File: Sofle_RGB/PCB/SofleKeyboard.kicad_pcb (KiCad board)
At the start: 2 copper layers, 143.4 x 111.8 mm, 97 parts, among them J1 LED, J2 4PIN, J3 OLED, J4 key leds, J5 backlight sel, J6 indicator bypass, P1 i2c_pin, P2 i2c_pin, SW1 SW_PUSH-MX_W_LED, SW10 SW_PUSH-MX_W_LED, SW11 SW_PUSH-MX_W_LED, SW12 SW_PUSH-MX_W_LED, SW13 SW_PUSH-MX_W_LED, SW14 SW_PUSH-MX_W_LED, SW15 SW_PUSH-MX_W_LED, SW16 SW_PUSH-MX_W_LED, SW17 SW_PUSH-MX_W_LED, SW18 SW_PUSH-MX_W_LED, SW19 SW_PUSH-MX_W_LED, SW2 SW_PUSH-MX_W_LED, SW20 SW_PUSH-MX_W_LED, SW21 SW_PUSH-MX_W_LED, SW22 SW_PUSH-MX_W_LED, SW23 SW_PUSH-MX_W_LED, SW24 SW_PUSH-MX_W_LED, SW25 Rotary_Encoder_Switch, SW26 SW_PUSH-MX_W_LED, SW27 SW_PUSH-MX_W_LED, SW28 SW_PUSH-MX_W_LED, SW29 SW_PUSH-MX_W_LED, SW3 SW_PUSH-MX_W_LED, SW30 SW_PUSH-MX_W_LED, SW4 SW_PUSH-MX_W_LED, SW5 SW_PUSH-MX_W_LED, SW6 SW_PUSH-MX_W_LED, SW7 SW_PUSH-MX_W_LED, SW8 SW_PUSH-MX_W_LED, SW9 SW_PUSH-MX_W_LED, U1 ProMicro

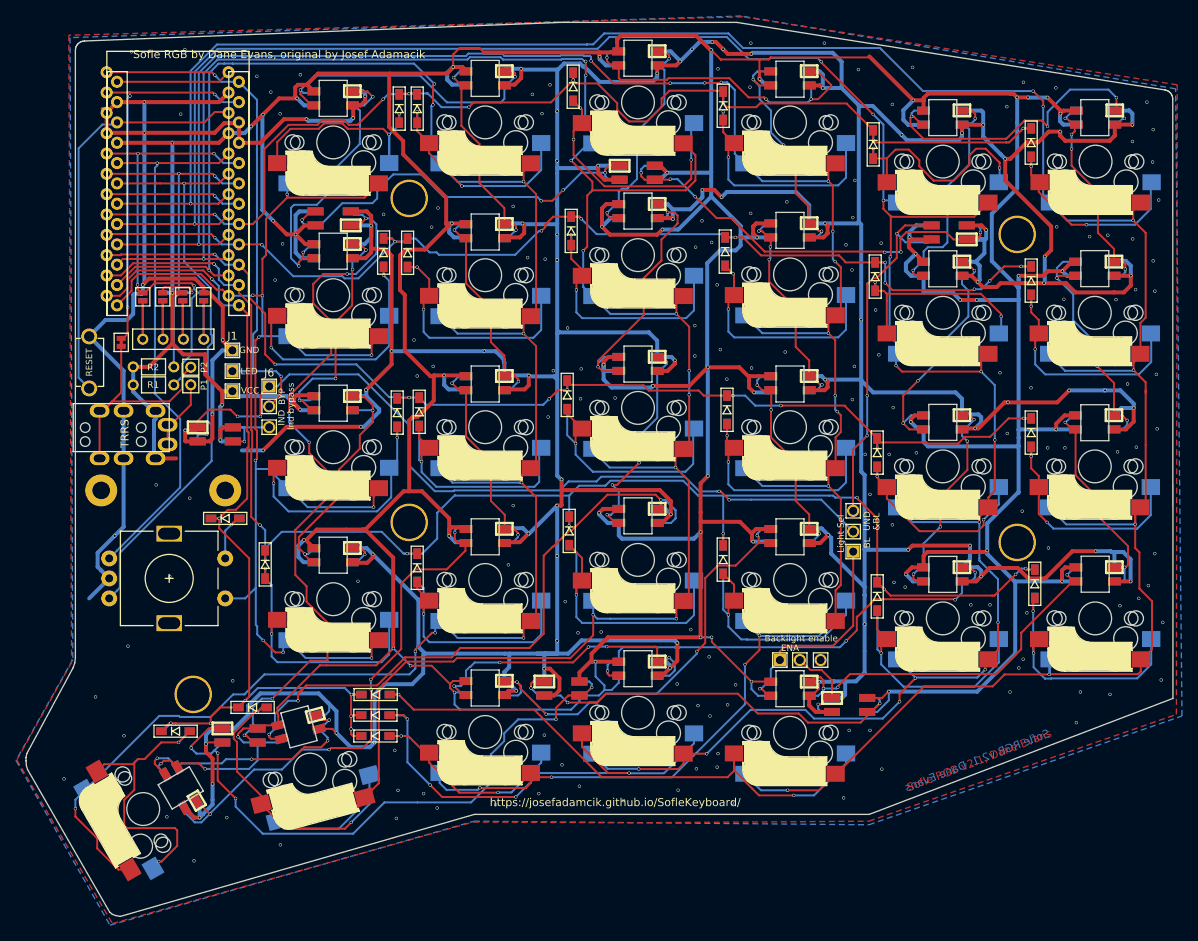
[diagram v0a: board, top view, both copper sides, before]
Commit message: Cleaned and retraced some GND tracks.
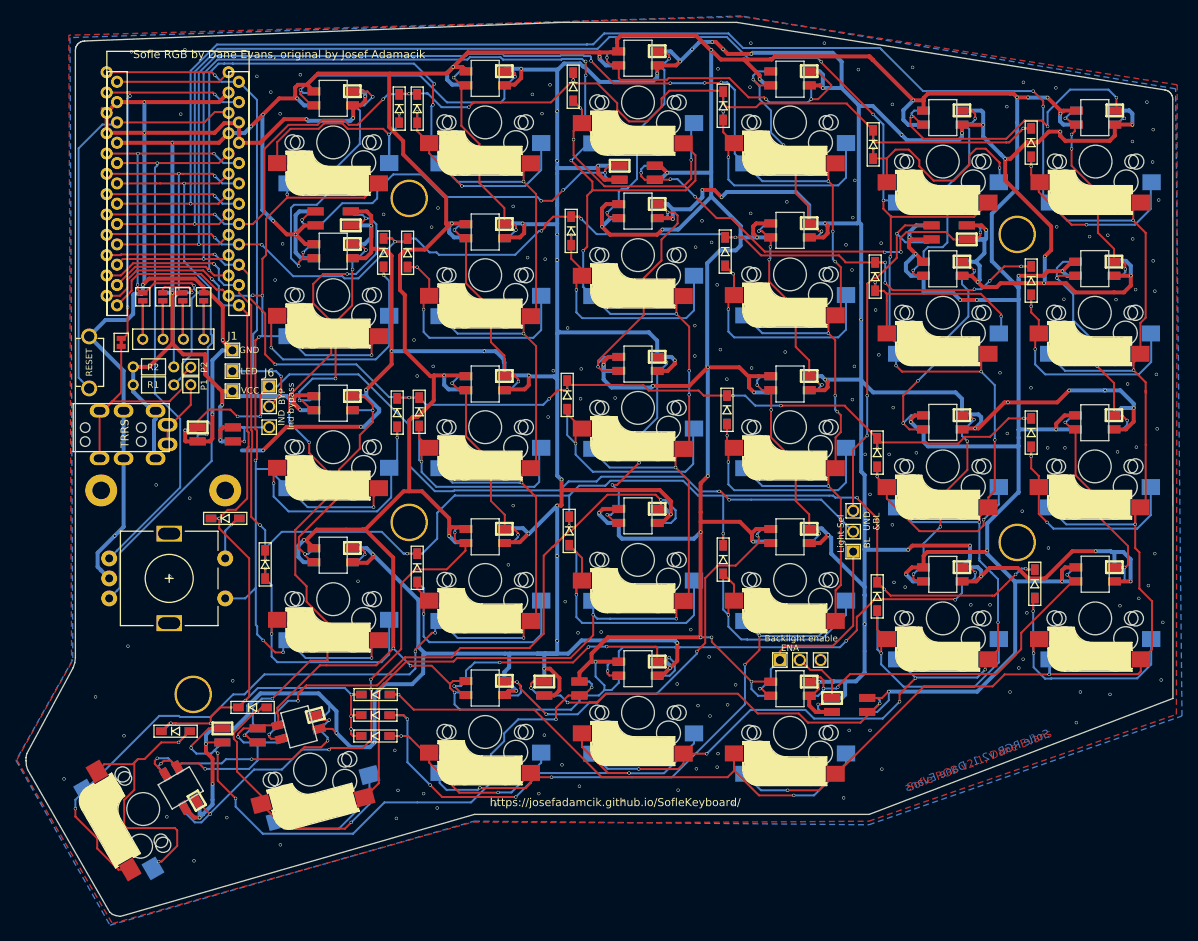
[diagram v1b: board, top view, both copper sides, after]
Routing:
- net VCC: track 928.4 -> 923.7 mm
- net GND: track 1001.1 -> 997.6 mm
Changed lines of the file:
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@@
     (thickness 1.6)
     (drawings 363)
-    (tracks 3681)
+    (tracks 3672)
     (zones 0)
     (modules 97)
@@
     (visible_elements 7FFFF7FF)
     (pcbplotparams
-      (layerselection 0x010f0_ffffffff)
+      (layerselection 0x010fc_ffffffff)
       (usegerberextensions true)
       (usegerberattributes false)
@@
       (psa4output false)
       (plotreference true)
-      (plotvalue true)
+      (plotvalue false)
       (plotinvisibletext false)
       (padsonsilk false)
-      (subtractmaskfromsilk false)
+      (subtractmaskfromsilk true)
       (outputformat 1)
       (mirror false)
@@
   (segment (start 134.749998 41.325012) (end 135.5 40.57501) (width 0.5) (layer B.Cu) (net 33))
   (via (at 153.8 39.29) (size 0.4) (drill 0.3) (layers F.Cu B.Cu) (net 33))
-  (segment (start 193.0125 44.7375) (end 187.525 39.25) (width 0.5) (layer F.Cu) (net 33))
   (via (at 173.806234 42.08623) (size 0.4) (drill 0.3) (layers F.Cu B.Cu) (net 33))
   (segment (start 174.595004 42.875) (end 173.841595 42.121591) (width 0.5) (layer B.Cu) (net 33))
   (segment (start 175.2 42.875) (end 174.595004 42.875) (width 0.5) (layer B.Cu) (net 33))
-  (segment (start 173.785002 42.064998) (end 173.806234 42.08623) (width 0.5) (layer F.Cu) (net 33))
-  (segment (start 173.785002 41.814998) (end 173.785002 42.064998) (width 0.5) (layer F.Cu) (net 33))
   (segment (start 118.1 83.475) (end 116.425 83.475) (width 0.5) (layer B.Cu) (net 33))
   (segment (start 114.662001 81.712001) (end 116.35 83.4) (width 0.5) (layer B.Cu) (net 33))
@@
   (segment (start 200.95 69.7) (end 206.1 69.7) (width 0.5) (layer B.Cu) (net 33))
   (segment (start 206.175 68.125) (end 206.175 85.925) (width 0.5) (layer B.Cu) (net 33))
-  (segment (start 167.75 38.44) (end 168.946 39.636) (width 0.25) (layer F.Cu) (net 33))
-  (segment (start 168.946 39.636) (end 168.946 39.65) (width 0.25) (layer F.Cu) (net 33))
   (segment (start 135.225 60.125) (end 135.325 60.125) (width 0.5) (layer F.Cu) (net 33))
   (segment (start 129.569998 63.4) (end 131.95 63.4) (width 0.5) (layer F.Cu) (net 33))
@@
   (segment (start 153.782 39.272) (end 153.8 39.29) (width 0.5) (layer F.Cu) (net 33))
   (segment (start 153.782 38.75) (end 153.782 39.272) (width 0.5) (layer F.Cu) (net 33))
-  (segment (start 173.785002 41.814998) (end 173.785002 39.710002) (width 0.25) (layer F.Cu) (net 33))
-  (segment (start 173.785002 41.125) (end 173.785002 41.814998) (width 0.25) (layer F.Cu) (net 33))
-  (segment (start 175.2 41.125) (end 173.785002 41.125) (width 0.25) (layer F.Cu) (net 33))
   (segment (start 171.265 78.115) (end 167.325 78.115) (width 0.5) (layer F.Cu) (net 33))
   (segment (start 172.475 79.325) (end 171.265 78.115) (width 0.5) (layer F.Cu) (net 33))
-  (segment (start 175.178801 39.374999) (end 187.400001 39.374999) (width 0.25) (layer F.Cu) (net 33))
-  (segment (start 187.400001 39.374999) (end 187.525 39.25) (width 0.25) (layer F.Cu) (net 33))
-  (segment (start 173.711 39.636) (end 173.785002 39.710002) (width 0.25) (layer F.Cu) (net 33))
-  (segment (start 168.946 39.636) (end 173.711 39.636) (width 0.25) (layer F.Cu) (net 33))
-  (segment (start 174.9178 39.636) (end 175.178801 39.374999) (width 0.25) (layer F.Cu) (net 33))
-  (segment (start 173.711 39.636) (end 174.9178 39.636) (width 0.25) (layer F.Cu) (net 33))
   (segment (start 154.602158 40.375) (end 156.2 40.375) (width 0.5) (layer B.Cu) (net 33))
   (segment (start 153.8 39.29) (end 153.8 39.572842) (width 0.5) (layer B.Cu) (net 33))
-  (segment (start 139.334 38.75) (end 156 38.75) (width 0.5) (layer F.Cu) (net 33))
   (segment (start 153.8 39.572842) (end 154.602158 40.375) (width 0.5) (layer B.Cu) (net 33))
-  (segment (start 138.7856 38.2016) (end 139.334 38.75) (width 0.25) (layer F.Cu) (net 33))
-  (segment (start 136.2964 38.2016) (end 138.7856 38.2016) (width 0.25) (layer F.Cu) (net 33))
-  (segment (start 135.5 40.57501) (end 135.5 38.998) (width 0.25) (layer F.Cu) (net 33))
-  (segment (start 135.5 38.998) (end 136.2964 38.2016) (width 0.25) (layer F.Cu) (net 33))
   (segment (start 194.3 44.45) (end 194.3 44.8) (width 0.5) (layer F.Cu) (net 33))
   (segment (start 194.85 43.9) (end 194.3 44.45) (width 0.5) (layer F.Cu) (net 33))
@@
   (segment (start 100.42262 68.79962) (end 100.400388 68.79962) (width 0.5) (layer F.Cu) (net 33))
   (segment (start 101.7 68.79962) (end 100.42262 68.79962) (width 0.5) (layer F.Cu) (net 33))
-  (segment (start 98.3 89.5) (end 100.873 89.5) (width 0.5) (layer F.Cu) (net 33))
   (segment (start 128 113.25) (end 125.883 115.367) (width 0.25) (layer F.Cu) (net 33))
   (segment (start 172.749999 98.837999) (end 172.849999 98.837999) (width 0.5) (layer F.Cu) (net 33))
@@
   (segment (start 211.6 104.85) (end 211.625 104.875) (width 0.5) (layer F.Cu) (net 33))
   (segment (start 211.975 103.125) (end 211.6 103.5) (width 0.5) (layer F.Cu) (net 33))
+  (segment (start 168.94821 39.63821) (end 167.75 38.44) (width 0.5) (layer F.Cu) (net 33))
+  (segment (start 171.84521 39.63821) (end 168.94821 39.63821) (width 0.5) (layer F.Cu) (net 33))
+  (segment (start 173.806234 41.599234) (end 171.84521 39.63821) (width 0.5) (layer F.Cu) (net 33))
+  (segment (start 173.806234 42.08623) (end 173.806234 41.599234) (width 0.5) (layer F.Cu) (net 33))
+  (segment (start 187.524999 39.249999) (end 187.993 39.718) (width 0.5) (layer F.Cu) (net 33))
+  (segment (start 175.319314 39.63821) (end 175.707525 39.249999) (width 0.5) (layer F.Cu) (net 33))
+  (segment (start 175.707525 39.249999) (end 187.524999 39.249999) (width 0.5) (layer F.Cu) (net 33))
+  (segment (start 171.84521 39.63821) (end 175.319314 39.63821) (width 0.5) (layer F.Cu) (net 33))
+  (segment (start 187.993 39.718) (end 187.525 39.25) (width 0.5) (layer F.Cu) (net 33))
+  (segment (start 193.0125 44.7375) (end 187.993 39.718) (width 0.5) (layer F.Cu) (net 33))
+  (segment (start 137.32501 38.75) (end 135.5 40.57501) (width 0.5) (layer F.Cu) (net 33))
+  (segment (start 156 38.75) (end 137.32501 38.75) (width 0.5) (layer F.Cu) (net 33))
   (segment (start 218.1 47.775) (end 218.475 47.775) (width 0.5) (layer F.Cu) (net 34))
   (segment (start 218.325 46.25) (end 218.1 46.025) (width 0.5) (layer B.Cu) (net 34))
@@
   (segment (start 192.218533 49.7205) (end 198.6915 49.7205) (width 0.5) (layer B.Cu) (net 34))
   (segment (start 187.948034 45.450001) (end 191.549016 49.050984) (width 0.5) (layer B.Cu) (net 34))
-  (segment (start 92.5 104.5) (end 90 107) (width 0.5) (layer B.Cu) (net 34))
   (segment (start 101.946161 133.165961) (end 102.878 134.0978) (width 0.25) (layer F.Cu) (net 34))
   (segment (start 101.915367 133.165961) (end 101.946161 133.165961) (width 0.25) (layer F.Cu) (net 34))
